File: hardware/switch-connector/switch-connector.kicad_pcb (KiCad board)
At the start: 2 copper layers, 40 x 27.9 mm, 10 parts, among them P1 12V, P2 Force off (NC), P3 12V Sensing, P4 Switches, P5 Enable on (NO), P6 HV-Relay

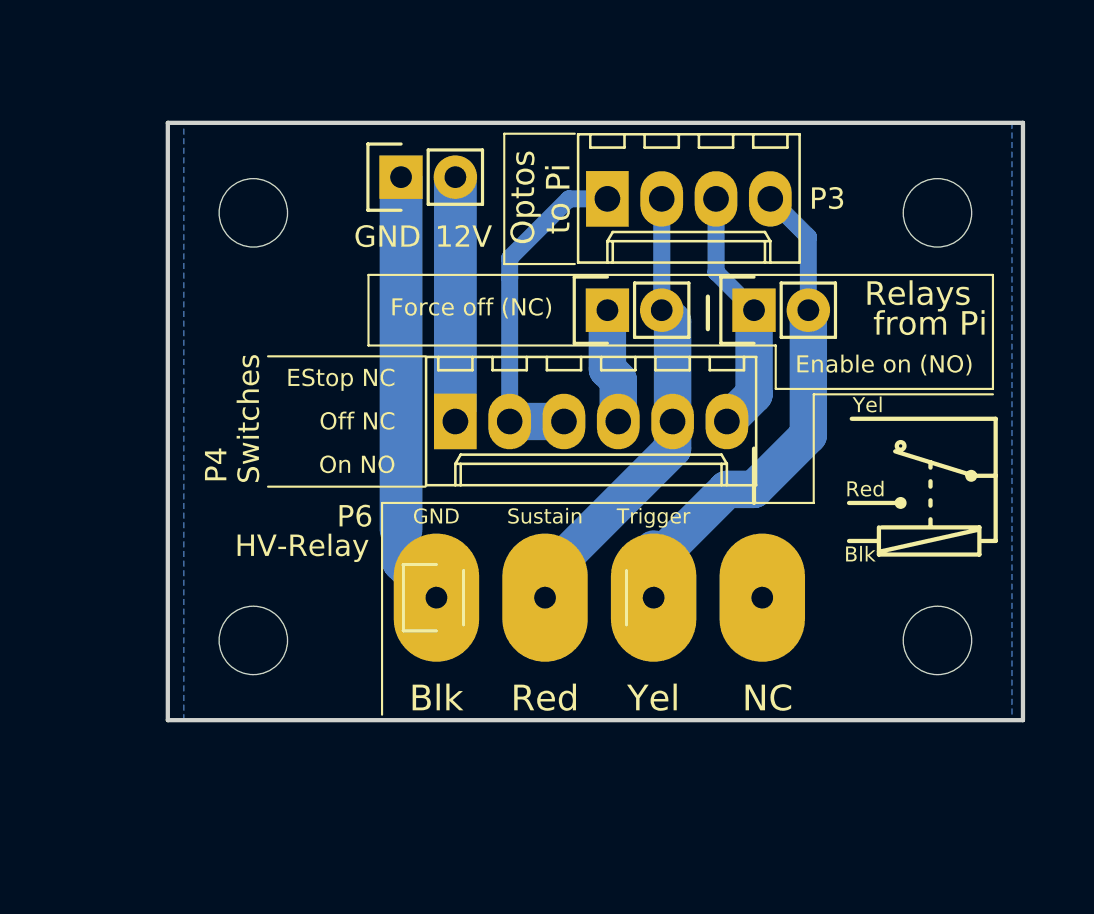
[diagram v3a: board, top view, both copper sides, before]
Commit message: Rounded corners.
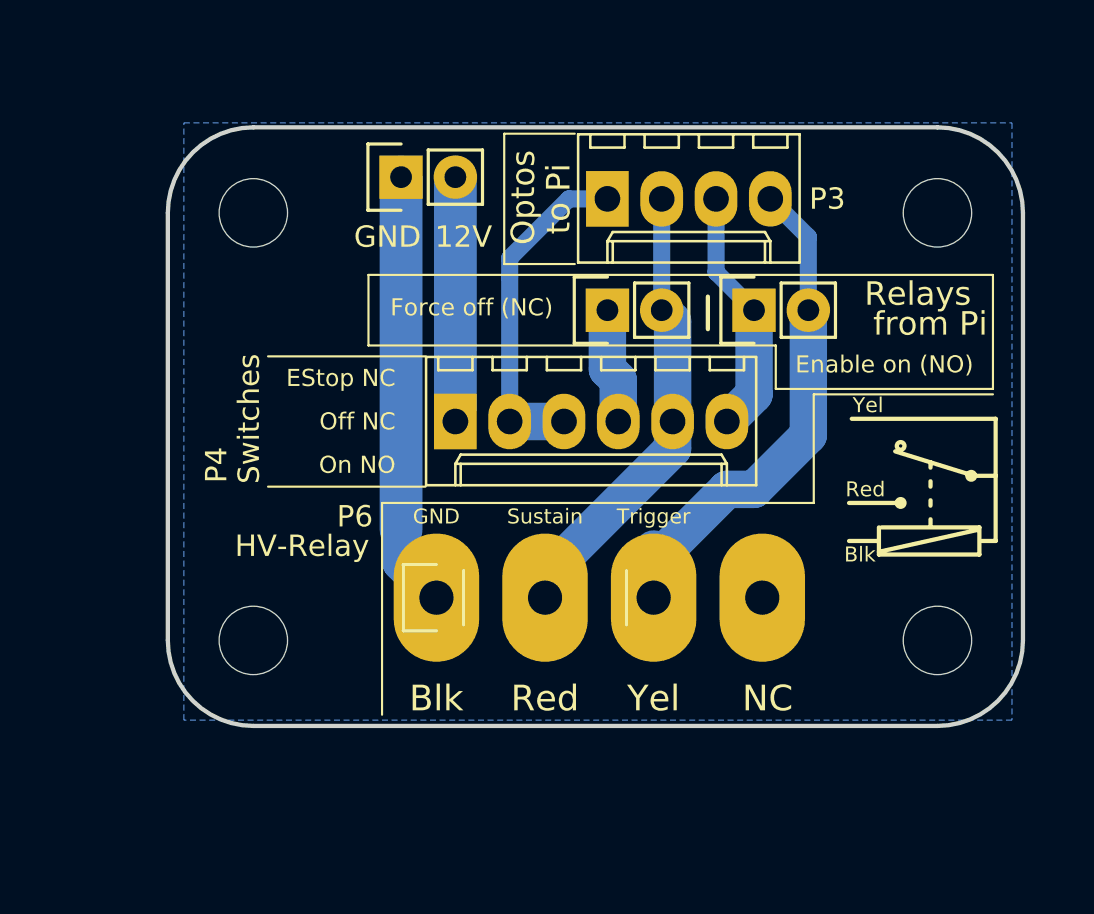
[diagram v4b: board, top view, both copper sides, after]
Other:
- board size 40 x 27.9 mm -> 40 x 28 mm
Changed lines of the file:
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@@
   (general
     (thickness 1.6)
-    (drawings 58)
+    (drawings 61)
     (tracks 35)
     (zones 0)
@@
   )
   (setup
-    (last_trace_width 1.75)
+    (last_trace_width 1.5)
     (user_trace_width 0.8)
     (user_trace_width 1.5)
@@
     (mod_text_size 1 1)
     (mod_text_width 0.15)
-    (pad_size 3.2 3.2)
-    (pad_drill 3.2)
+    (pad_size 6 4)
+    (pad_drill 1.6)
     (pad_to_mask_clearance 0.2)
     (aux_axis_origin 0 0)
+    (grid_origin 194 98)
     (visible_elements FFFFFF7F)
     (pcbplotparams
@@
     (fp_line (start -1.55 0) (end -1.55 -1.55) (layer F.SilkS) (width 0.15))
     (fp_line (start -1.55 -1.55) (end 1.55 -1.55) (layer F.SilkS) (width 0.15))
-    (pad 1 thru_hole oval (at 0 0 90) (size 6 4) (drill 1.016) (layers *.Cu *.Mask F.SilkS)
+    (pad 1 thru_hole oval (at 0 0 90) (size 6 4) (drill 1.6) (layers *.Cu *.Mask F.SilkS)
       (net 2 GND))
-    (pad 2 thru_hole oval (at 0 5.08 90) (size 6 4) (drill 1.016) (layers *.Cu *.Mask F.SilkS)
+    (pad 2 thru_hole oval (at 0 5.08 90) (size 6 4) (drill 1.6) (layers *.Cu *.Mask F.SilkS)
       (net 6 /Sustain))
-    (pad 3 thru_hole oval (at 0 10.16 90) (size 6 4) (drill 1.016) (layers *.Cu *.Mask F.SilkS)
+    (pad 3 thru_hole oval (at 0 10.16 90) (size 6 4) (drill 1.6) (layers *.Cu *.Mask F.SilkS)
       (net 7 /Trigger))
-    (pad 4 thru_hole oval (at 0 15.24 90) (size 6 4) (drill 1.016) (layers *.Cu *.Mask F.SilkS))
+    (pad 4 thru_hole oval (at 0 15.24 90) (size 6 4) (drill 1.6) (layers *.Cu *.Mask F.SilkS))
     (model Pin_Headers.3dshapes/Pin_Header_Straight_1x04.wrl
       (offset (xyz 0 -3.809999942779541 0))
@@
     )
   )
+  (gr_arc (start 194 122) (end 194 126) (angle -90) (layer Edge.Cuts) (width 0.2))
+  (gr_arc (start 162 122) (end 158 122) (angle -90) (layer Edge.Cuts) (width 0.2))
+  (gr_arc (start 162 102) (end 162 98) (angle -90) (layer Edge.Cuts) (width 0.2))
+  (gr_arc (start 194 102) (end 198 102) (angle -90) (layer Edge.Cuts) (width 0.2))
   (gr_line (start 188.214 110.49) (end 188.214 115.57) (layer F.SilkS) (width 0.1))
   (gr_line (start 188.214 110.49) (end 196.596 110.49) (layer F.SilkS) (width 0.1))
@@
     (effects (font (size 1.2 1.2) (thickness 0.2)))
   )
-  (gr_line (start 185.42 115.57) (end 185.42 113.03) (layer F.SilkS) (width 0.2))
   (gr_text "On NO" (at 168.656 113.792) (layer F.SilkS)
     (effects (font (size 0.8 0.8) (thickness 0.1)) (justify right))
@@
     (effects (font (size 1.2 1.2) (thickness 0.2)))
   )
-  (gr_line (start 158 125.73) (end 158 97.79) (layer Edge.Cuts) (width 0.2))
-  (gr_line (start 198 125.73) (end 158 125.73) (layer Edge.Cuts) (width 0.2))
-  (gr_line (start 198 97.79) (end 198 125.73) (layer Edge.Cuts) (width 0.2))
-  (gr_line (start 158 97.79) (end 198 97.79) (layer Edge.Cuts) (width 0.2))
+  (gr_line (start 158 122) (end 158 102) (layer Edge.Cuts) (width 0.2))
+  (gr_line (start 194 126) (end 162 126) (layer Edge.Cuts) (width 0.2))
+  (gr_line (start 198 102) (end 198 122) (layer Edge.Cuts) (width 0.2))
+  (gr_line (start 162 98) (end 194 98) (layer Edge.Cuts) (width 0.2))
   (segment (start 178.562 106.553) (end 178.562 109.319) (width 1.75) (layer B.Cu) (net 1))
   (segment (start 178.562 109.319) (end 179.07 109.827) (width 1.75) (layer B.Cu) (net 1))

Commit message: Add screw terminal for 12V
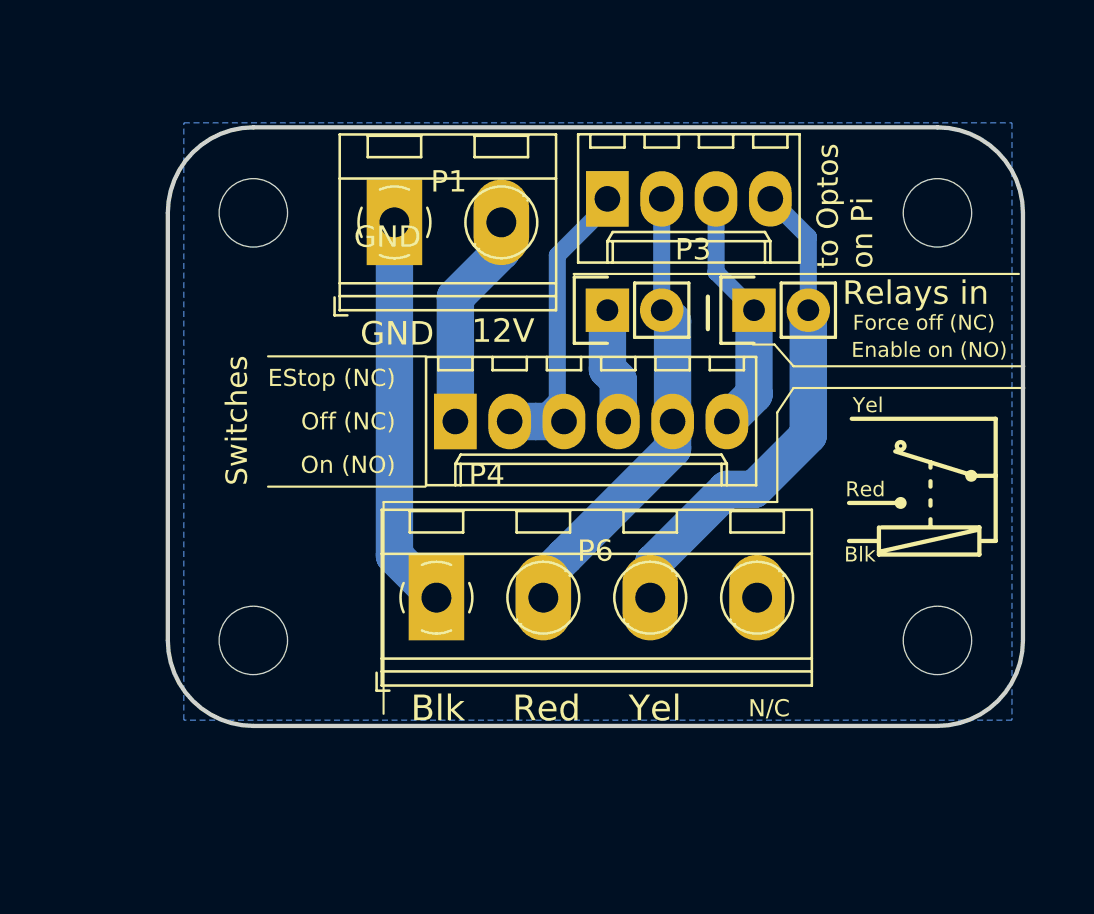
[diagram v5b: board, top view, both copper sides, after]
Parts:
- P1: footprint Pin_Headers:Pin_Header_Straight_1x02 -> TerminalBlock_RND:TerminalBlock_RND_205-00045_Pitch5.00mm
- P6: footprint Pin_Headers:Pin_Header_Straight_1x04 -> TerminalBlock_RND:TerminalBlock_RND_205-00047_Pitch5.00mm
- moved P1 2.14 mm to (168.6, 102.4), turned to 0 degrees
- turned P6 to 0 degrees
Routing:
- net /Trigger: track 30.4 -> 24.8 mm
- net GND: track 20.4 -> 18.4 mm
- net /switch-box/Sense-E-Stop: track 15.9 -> 14.3 mm
- net /Sustain: track 23.8 -> 24.5 mm
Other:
- board text added: "12V"
- board text added: "EStop (NC)"
- board text added: "N/C"
- board text added: "Off (NC)"
- board text added: "On (NO)"
- board text added: "Relays in"
- board text added: "to Optos on Pi"
- board text removed: "EStop NC"
- board text removed: "NC"
- board text removed: "Off NC"
- board text removed: "On NO"
- board text removed: "Optos"
- board text removed: "Relays"
- board text removed: "Sustain"
- board text removed: "Trigger"
- board text removed: "from Pi"
- board text removed: "to Pi"

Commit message: Some tweaking (but about to be changed for refined design)
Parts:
- P3: footprint Connectors_Molex:Molex_KK-6410-04_04x2.54mm_Straight -> Connectors_JST:JST_XH_B04B-XH-A_04x2.50mm_Straight
- P4: footprint Connectors_Molex:Molex_KK-6410-06_06x2.54mm_Straight -> Connectors_JST:JST_XH_B06B-XH-A_06x2.50mm_Straight
- moved P3 1.17 mm to (179.6, 100.9)
- moved P4 0.43 mm to (171.5, 111.3)
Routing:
- net /switch-box/Sense-E-Stop: track 14.3 -> 15.8 mm
- net /Sustain: track 24.5 -> 25.3 mm
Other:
- board text added: "github.com/hzeller/sparkle-switch"
- board text added: "to Optos"
- board text removed: "to Optos on Pi"

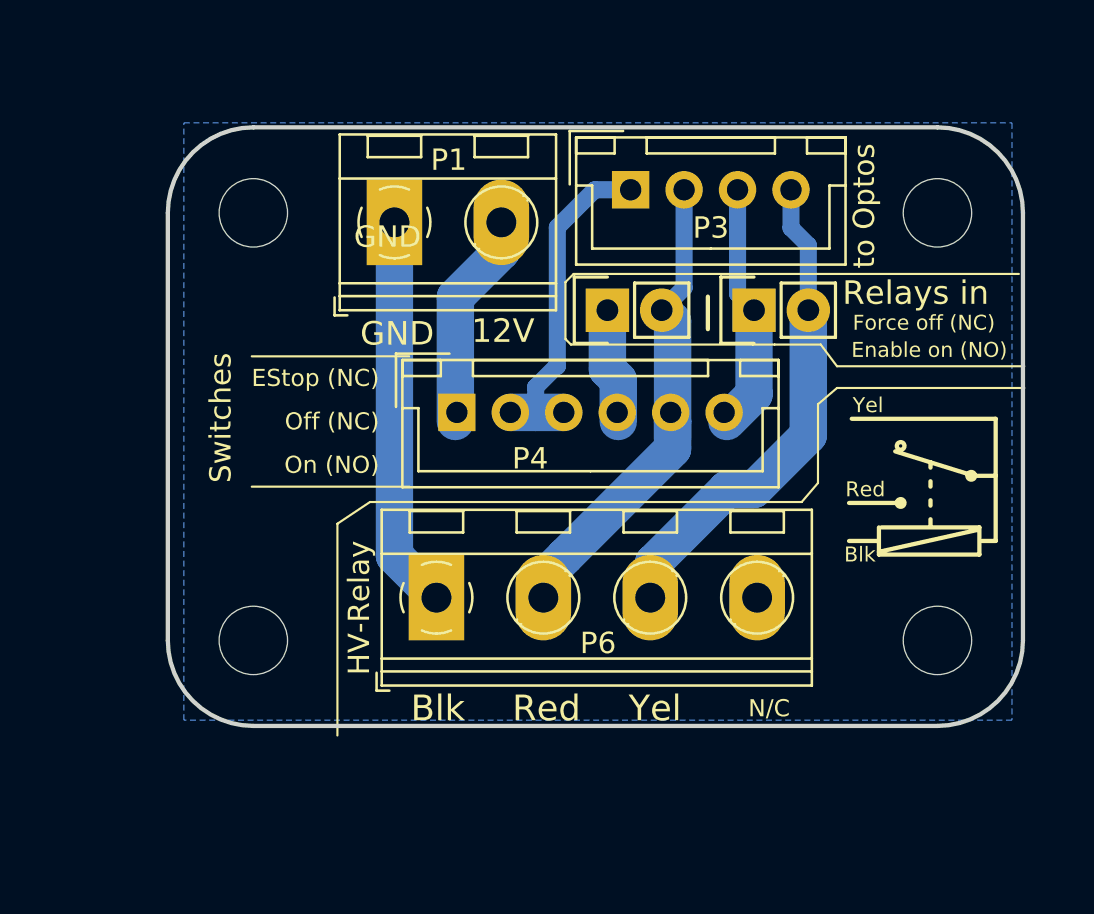
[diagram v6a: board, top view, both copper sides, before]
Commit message: First version of the PCB using the IDC connector.
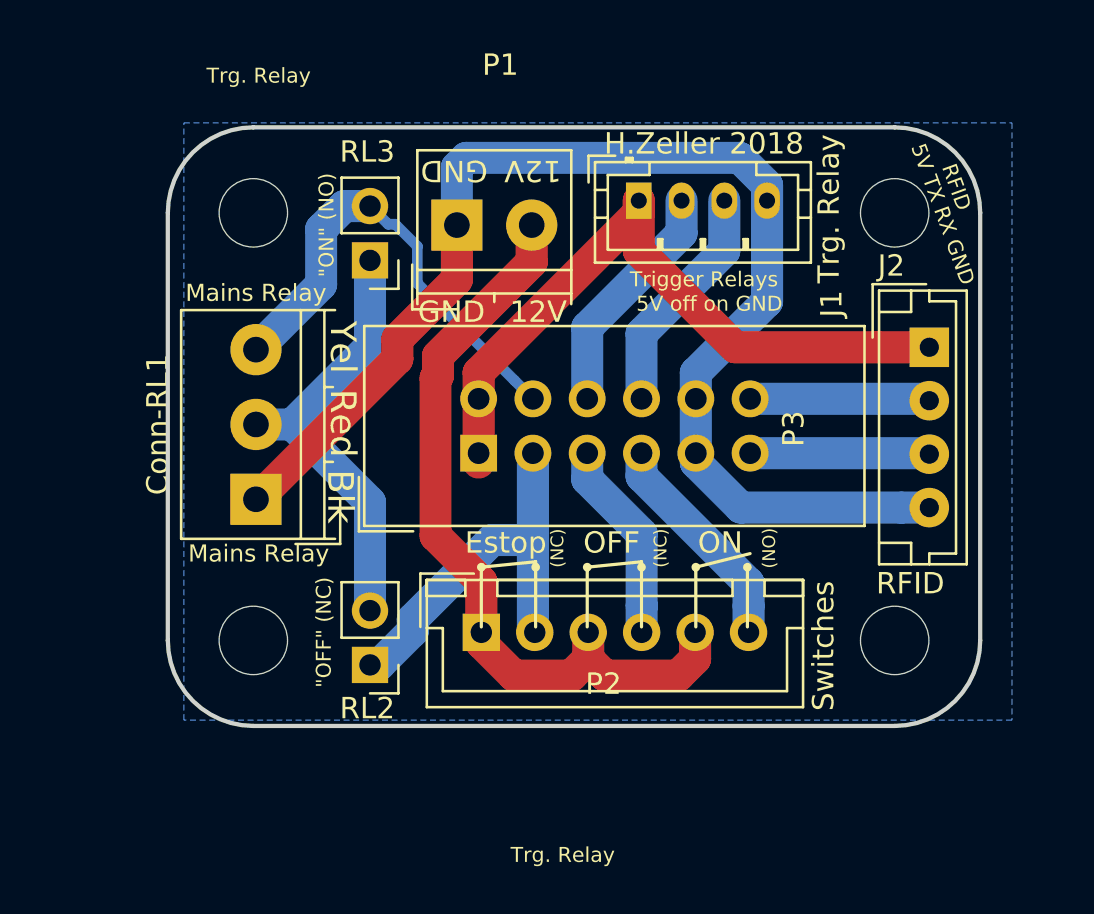
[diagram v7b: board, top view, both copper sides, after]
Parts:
- removed P4: Switches, Connectors_JST:JST_XH_B06B-XH-A_06x2.50mm_Straight
- removed P5: Enable on (NO), Pin_Headers:Pin_Header_Straight_1x02
- removed P6: HV-Relay, TerminalBlock_RND:TerminalBlock_RND_205-00047_Pitch5.00mm
- added Conn-RL1: HV-Relay, TerminalBlock_4UCON:TerminalBlock_4UCON_19963_03x3.5mm_Straight, F.Cu at (162.1, 115.4)
- added J1: Relay Control, Connectors_JST:JST_PH_B4B-PH-K_04x2.00mm_Straight, F.Cu at (180.0, 101.4)
- added J2: RFID connect, Connectors_JST:JST_EH_B04B-EH-A_04x2.50mm_Straight, F.Cu at (193.6, 108.3)
- added RL2: Trigger off (NC), Pin_Headers:Pin_Header_Straight_1x02_Pitch2.54mm, F.Cu at (167.5, 123.1)
- added RL3: Enable On (NO), Pin_Headers:Pin_Header_Straight_1x02_Pitch2.54mm, F.Cu at (167.5, 104.2)
- P1: footprint TerminalBlock_RND:TerminalBlock_RND_205-00045_Pitch5.00mm -> TerminalBlock_4UCON:TerminalBlock_4UCON_19963_02x3.5mm_Straight
- P2: value Force off (NC) -> Switches; footprint Pin_Headers:Pin_Header_Straight_1x02 -> Connectors_JST:JST_XH_B06B-XH-A_06x2.50mm_Straight
- P3: value 12V Sensing -> Pi; footprint Connectors_JST:JST_XH_B04B-XH-A_04x2.50mm_Straight -> Connectors_IDC:IDC-Header_2x06_Pitch2.54mm_Straight
- moved P2 16.2 mm to (172.7, 121.6), turned to 0 degrees
- moved P3 14.2 mm to (172.5, 113.2), turned to 90 degrees
- moved P1 2.92 mm to (171.5, 102.6)
- moved REF** 2.00 mm to (192.0, 122.0)
- moved REF** 2.00 mm to (192.0, 102.0)
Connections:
- P2 pad 1: Net-(P2-Pad1) -> +12V
- P2 pad 2: /Sustain -> /switch-box/Sense-EStop
- P3 pad 1: /switch-box/Sense-E-Stop -> +5V
- P3 pad 2: /Sustain -> +5V
- P3 pad 3: /switch-box/Sense-On -> /switch-box/Sense-EStop
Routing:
- net GND: track 18.4 -> 60.8 mm
- net +5V: track 0.00 -> 33.2 mm
- net +12V: track 11.2 -> 36.4 mm
- net /switch-box/Sense-EStop: track 0.00 -> 18.8 mm
- net /switch-box/Sense-E-Stop: track 15.8 -> 0.00 mm
- net /switch-box/Sense-On: track 11.7 -> 0.00 mm
- net /switch-box/RL-Trigger-Off: track 0.00 -> 11.1 mm
- net /switch-box/RL-Trigger-On: track 0.00 -> 10.9 mm
- net /switch-box/But-On: track 0.00 -> 10.5 mm
- net /switch-box/But-Off: track 0.00 -> 9.44 mm
- net /switch-box/TX: track 0.00 -> 8.42 mm
- net /switch-box/RX: track 0.00 -> 8.40 mm
- net Net-(P2-Pad1): track 5.42 -> 0.00 mm
- net /Sustain: track 25.3 -> 21.1 mm
- net /Trigger: track 24.9 -> 22.0 mm
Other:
- board size 40 x 28 mm -> 38 x 28 mm
- net class Default: clearance 0.25 -> 0.4
- rule trace_clearance: 0.25 -> 0.4
- board text added: ""OFF" (NC)"
- board text added: ""ON" (NO)"
- board text added: "(NC)"
- board text added: "(NO)"
- board text added: "5V TX RX GND"
- board text added: "5V off on GND"
- board text added: "Estop"
- board text added: "H.Zeller 2018"
- board text added: "Mains Relay"
- board text added: "OFF"
- board text added: "ON"
- board text added: "RFID"
- board text added: "Switches"
- board text added: "Trg. Relay"
- board text added: "Trigger Relays"
- board text removed: "EStop (NC)"
- board text removed: "N/C"
- board text removed: "Off (NC)"
- board text removed: "On (NO)"
- board text removed: "Relays in"
- board text removed: "github.com/hzeller/sparkle-switch"
- board text removed: "to Optos"
